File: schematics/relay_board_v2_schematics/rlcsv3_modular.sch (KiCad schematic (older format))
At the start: 12 parts, among them P1 ACT_PWR, P2 CONN_01X09, P3 ACTUATOR

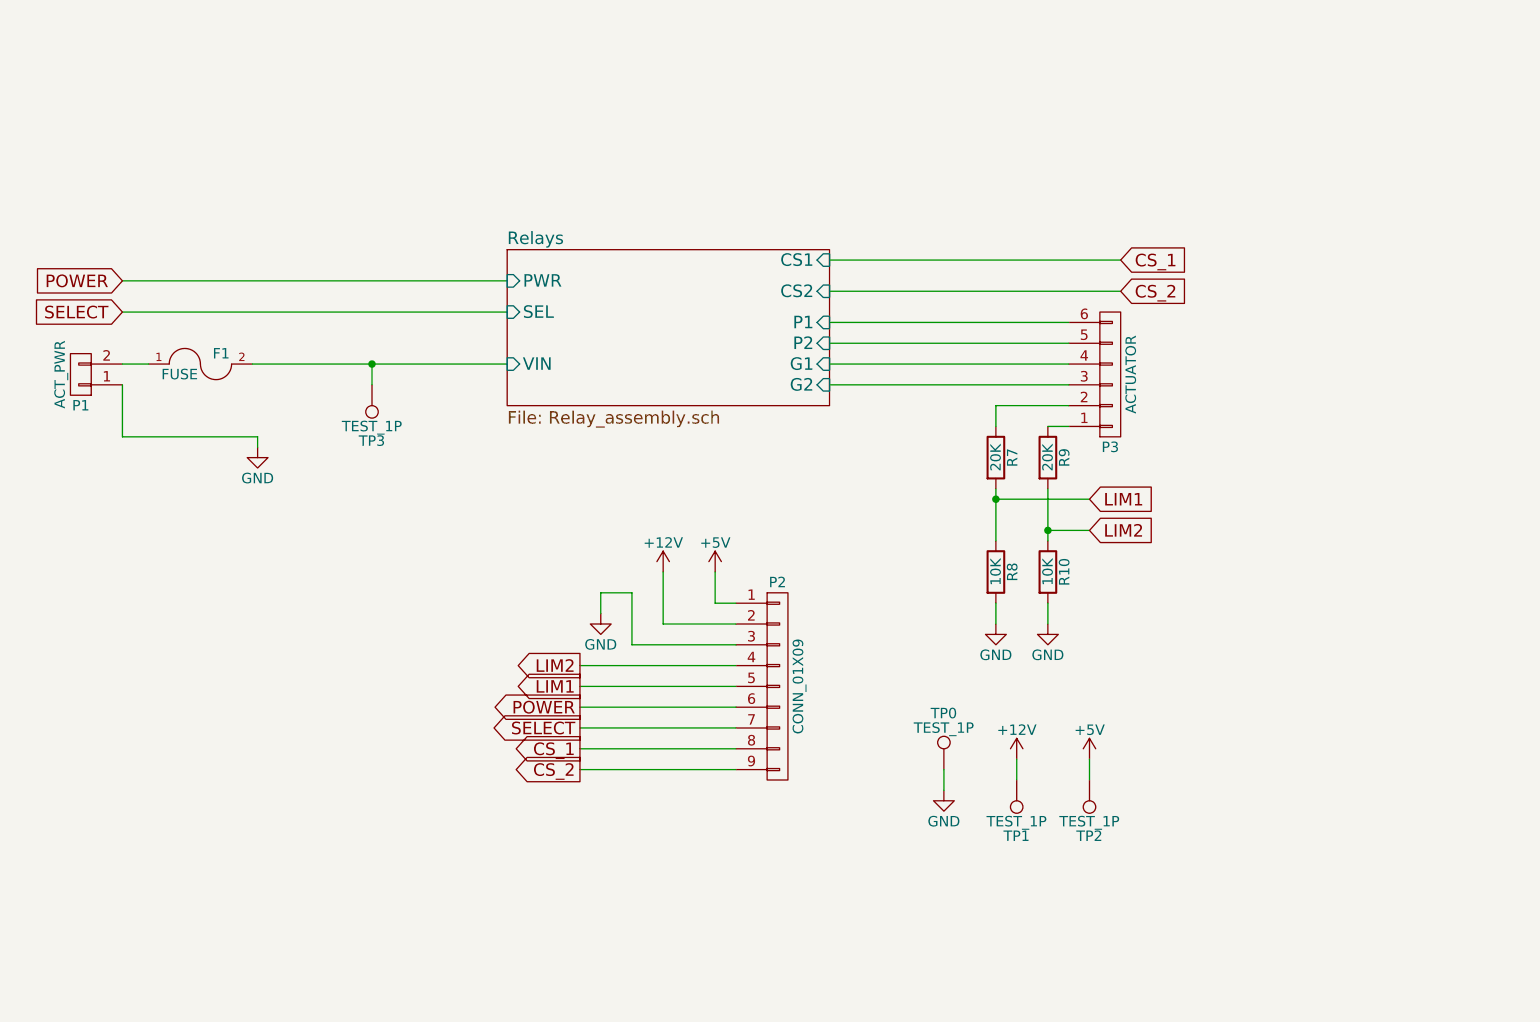
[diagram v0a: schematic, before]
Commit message: Add changes for wire cleanup for RLCS
Implement I2C protocol for board communication
Add Dip[ switch, programming header and pic to enable I2C

Signed-off-by: Aidan Ha <qbha@edu.uwaterloo.ca>
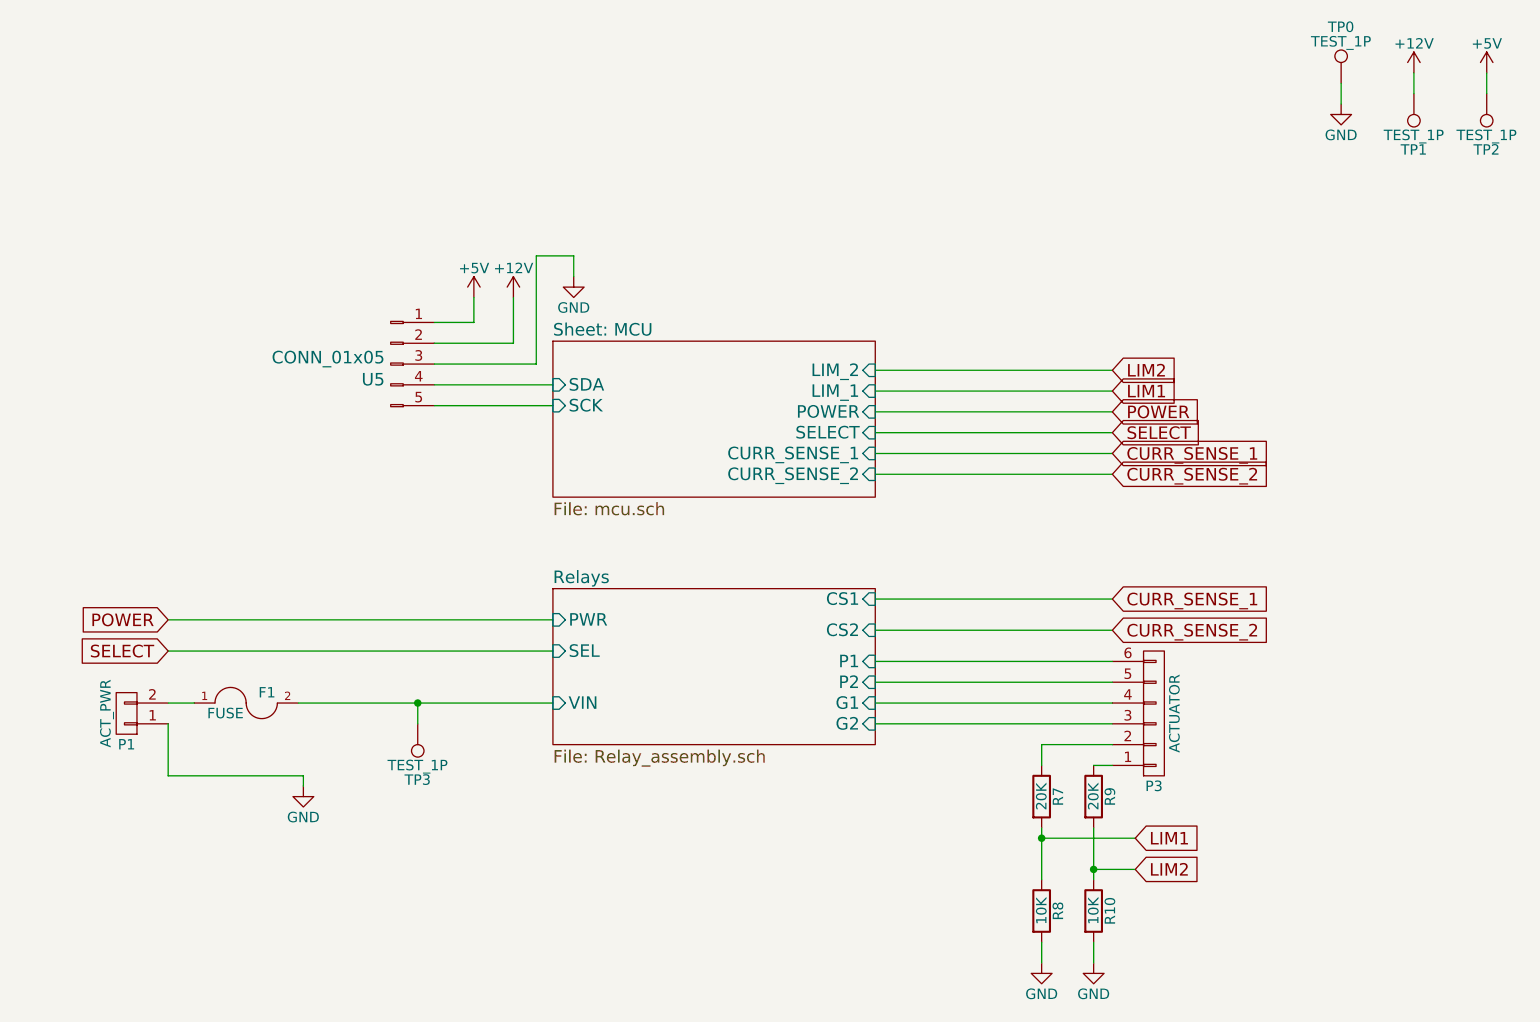
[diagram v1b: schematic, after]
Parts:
- removed P2: CONN_01X09, Socket_Strips:Socket_Strip_Straight_1x09_Pitch2.54mm, symbol rlcsv3_modular-rescue:CONN_01X09
- added U5: CONN_01x05, symbol rlcsv3_modular-rescue:CONN_01x05
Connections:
- net +12V: now also U5.2
- net +5V: now also U5.1
- net GND: now also U5.3
- new net Sheet: MCU/SCK: U5.5
- new net Sheet: MCU/SDA: U5.4
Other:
- moved on the sheet: F1, P1, P3, R10, R7, R8, R9, TP0, TP1, TP2, TP3
